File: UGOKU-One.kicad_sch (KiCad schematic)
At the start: 86 parts, among them J1 Conn_01x04, J10 Conn_01x02, J11 USB_C_Receptacle_USB2.0_16P, J12 Conn_01x02, J13 Conn_01x02, J2 SERVO, J3 Conn_02x03_Odd_Even, J4 Conn_01x10, J5 SERVO, J6 Conn_01x02, J8 DAC, J9 ADC, Q1 NMOS, Q2 SS8050, Q3 SS8050, SW1 SW_DIP_x02, SW2 SW_SPDT, SW4 SW_Push, SW6 SW_Push, U1 AMS1117-3.3, U2 CP2102N-A02-GQFN28, U3 TB67H450FNG_EL, U4 K7805M/M78AR05, U5 ESP32-WROOM-32E, U8 TB67H450FNG_EL

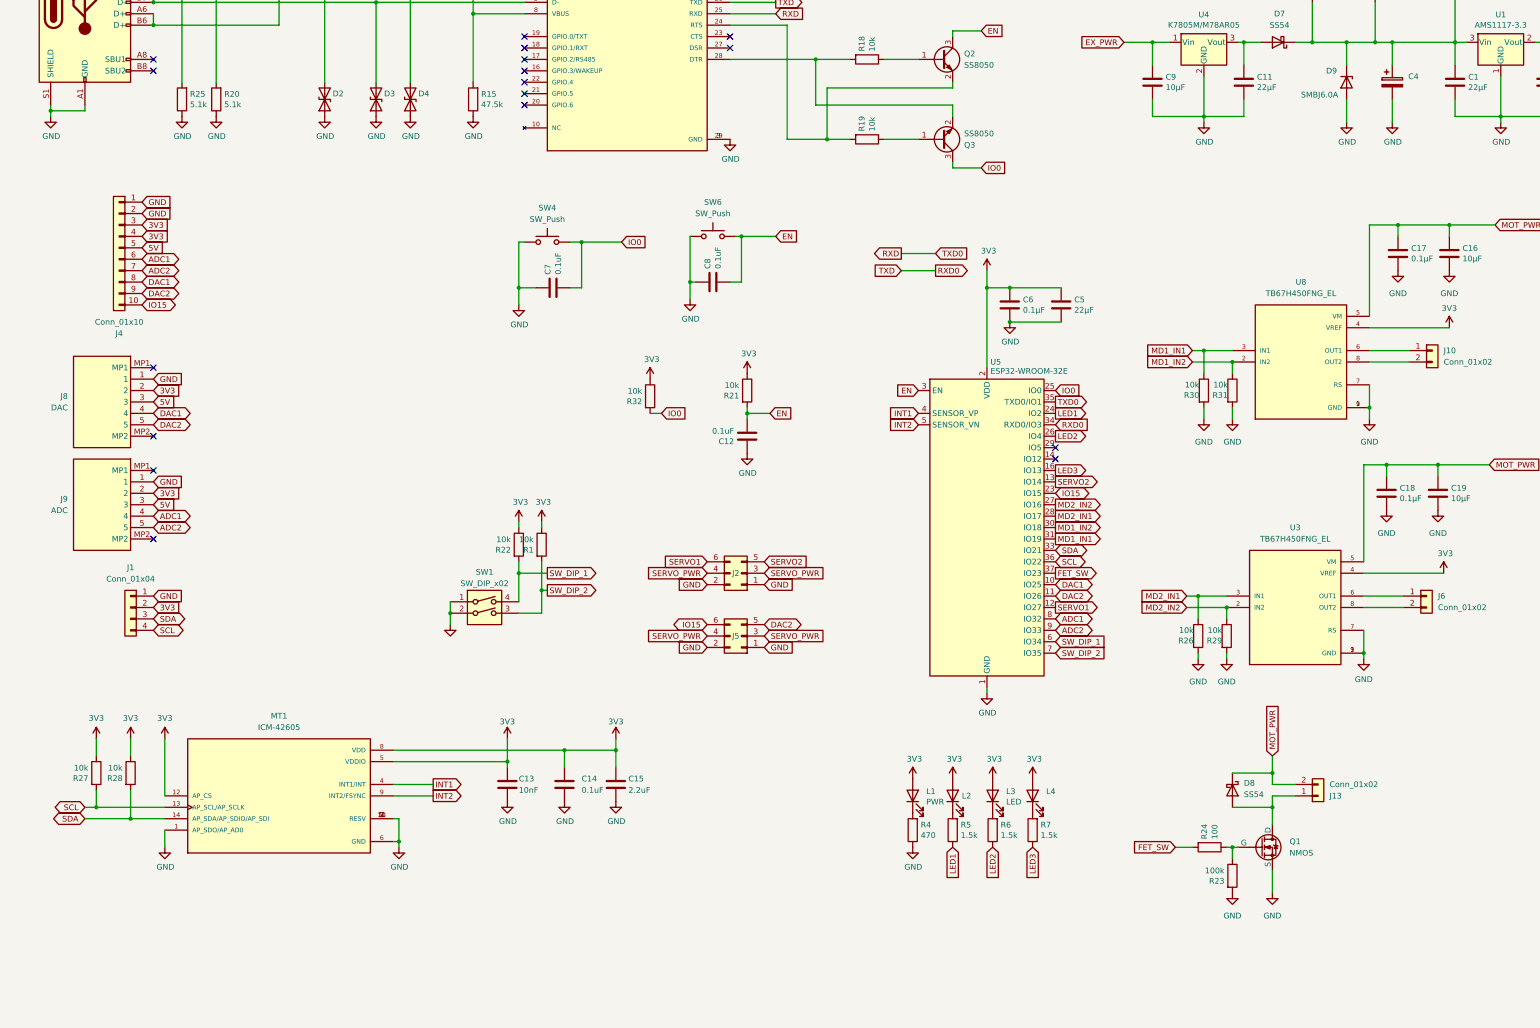
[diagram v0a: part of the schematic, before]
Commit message: 5VラインのコンデンサとTVSダイオードの配線を実施 IMUをBMI270に戻し
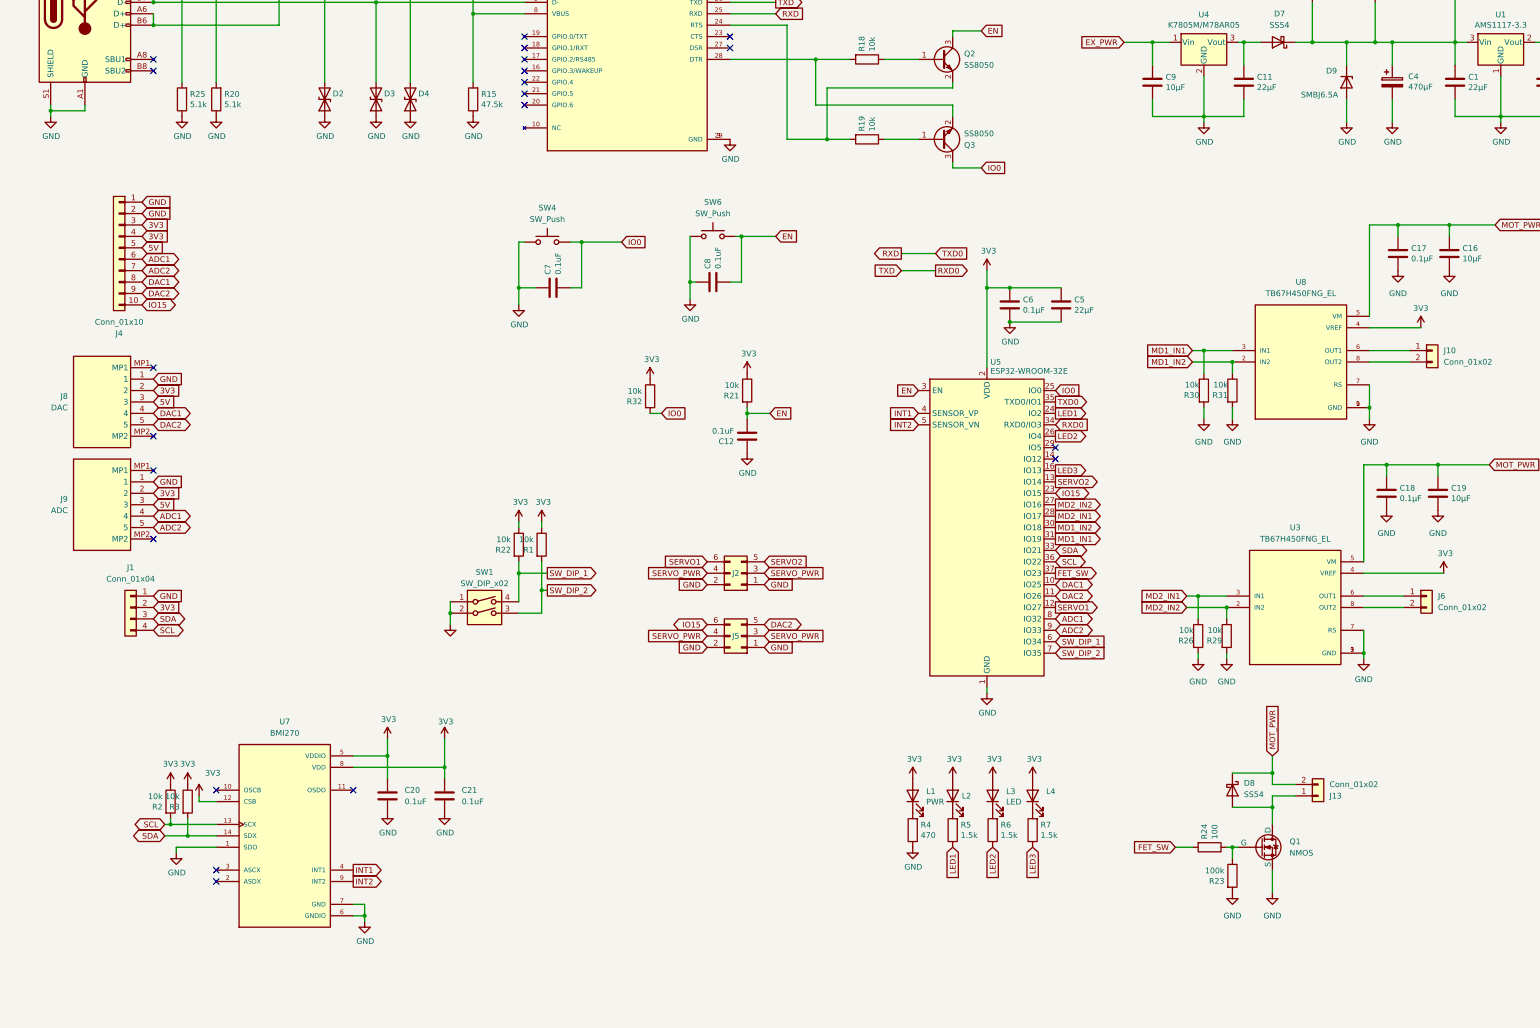
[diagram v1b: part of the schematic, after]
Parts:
- removed C13: 10nF, Capacitor_SMD:C_0402_1005Metric, symbol Device:C
- removed C14: 0.1uF, Capacitor_SMD:C_0402_1005Metric, symbol Device:C
- removed C15: 2.2uF, Capacitor_SMD:C_0402_1005Metric, symbol Device:C
- removed MT1: ICM-42605, 0_UGOKU-One_Lib:XDCR_ICM-42605, symbol ICM-42605:ICM-42605
- removed R27, R28: 10k, Resistor_SMD:R_0402_1005Metric, symbol Device:R
- added C20, C21: 0.1uF, Capacitor_SMD:C_0402_1005Metric, symbol Device:C
- added R2, R3: 10k, Resistor_SMD:R_0402_1005Metric, symbol Device:R
- added U7: BMI270, 0_UGOKU-One_Lib:XDCR_BMI270, symbol BMI270:BMI270
- C4: value C_Polarized -> 470μF; footprint Capacitor_SMD:CP_Elec_5x5.4 -> Capacitor_SMD:CP_Elec_6.3x7.7
- D9: value SMBJ6.0A -> SMBJ6.5A
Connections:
- net 3V3: now also C20.1, C21.1, R2.1, R3.1, U7.12 (CSB), U7.5 (VDDIO), U7.8 (VDD)
- net GND: now also C20.2, C21.2, U7.1 (SDO), U7.6 (GNDIO), U7.7 (GND)
- net INT1: now also U7.4 (INT1)
- net INT2: now also U7.9 (INT2)
- net SCL: now also R2.2, U7.13 (SCX)
- net SDA: now also R3.2, U7.14 (SDX)
- no-connect marks 24 -> 28

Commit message: ベタGNDとviaを修正
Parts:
- J4: footprint Connector_PinHeader_2.54mm:PinHeader_1x10_P2.54mm_Vertical -> Connector_PinSocket_2.54mm:PinSocket_1x10_P2.54mm_Vertical
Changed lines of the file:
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@@
 			)
 		)
-		(property "Footprint" "Connector_PinHeader_2.54mm:PinHeader_1x10_P2.54mm_Vertical"
+		(property "Footprint" "Connector_PinSocket_2.54mm:PinSocket_1x10_P2.54mm_Vertical"
 			(at 132.08 186.69 0)
 			(effects

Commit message: MD周りのベタ, viaを修正 BOM,CPLファイルを整備
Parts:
- C12, C20, C21, C3, C7, C8: value 0.1uF -> 0.1μF
- C2: value 22uF -> 22μF
- J2, J5: value SERVO -> Conn_02x03_Odd_Even
- J8: value DAC -> Harting-Conn
- J9: value ADC -> Harting-Conn
- L2: value IO2 -> LED
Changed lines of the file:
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@@
 			)
 		)
-		(property "Value" "IO2"
+		(property "Value" "LED"
 			(at 320.4972 309.9308 90)
 			(effects
@@
 			)
 		)
-		(property "Value" "SERVO"
+		(property "Value" "Conn_02x03_Odd_Even"
 			(at 269.24 266.7 0)
 			(effects
@@
 			)
 		)
-		(property "Value" "0.1uF"
+		(property "Value" "0.1μF"
 			(at 208.28 309.8799 0)
 			(effects
@@
 			)
 		)
-		(property "Value" "SERVO"
+		(property "Value" "Conn_02x03_Odd_Even"
 			(at 269.24 252.73 0)
 			(effects
@@
 			)
 		)
-		(property "Value" "22uF"
+		(property "Value" "22μF"
 			(at 279.4 102.8699 0)
 			(effects
@@
 			)
 		)
-		(property "Value" "0.1uF"
+		(property "Value" "0.1μF"
 			(at 290.83 102.8699 0)
 			(effects
@@
 		(on_board yes)
 		(dnp no)
-		(fields_autoplaced yes)
 		(property "Reference" "J9"
 			(at 120.65 242.5699 0)
@@
 			)
 		)
-		(property "Value" "ADC"
+		(property "Value" "Harting-Conn"
 			(at 120.65 245.1099 0)
 			(effects
@@
 			)
 		)
-		(property "Value" "DAC"
+		(property "Value" "Harting-Conn"
 			(at 120.65 222.2499 0)
 			(effects
@@
 			)
 		)
-		(property "Value" "0.1uF"
+		(property "Value" "0.1μF"
 			(at 265.303 191.389 0)
 			(effects
@@
 			)
 		)
-		(property "Value" "0.1uF"
+		(property "Value" "0.1μF"
 			(at 195.58 309.8799 0)
 			(effects
@@
 			)
 		)
-		(property "Value" "0.1uF"
+		(property "Value" "0.1μF"
 			(at 268.859 227.457 0)
 			(effects
@@
 			)
 		)
-		(property "Value" "0.1uF"
+		(property "Value" "0.1μF"
 			(at 229.743 192.659 0)
 			(effects

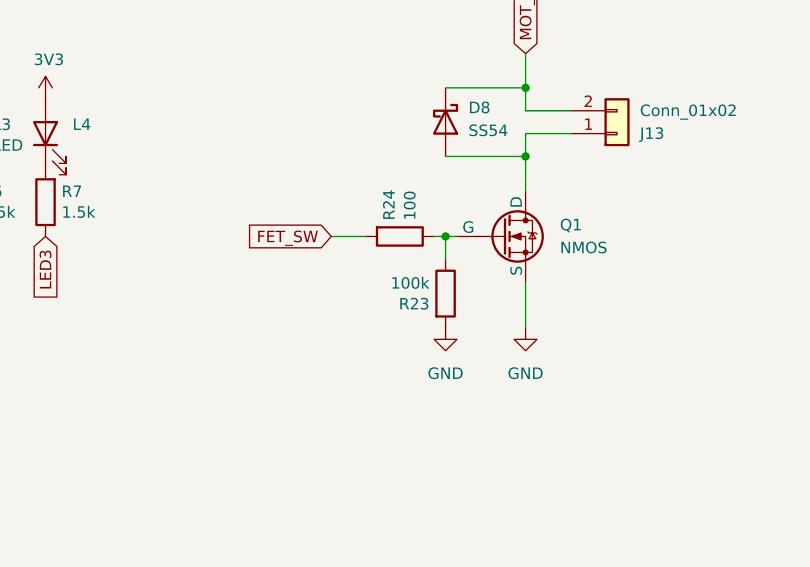
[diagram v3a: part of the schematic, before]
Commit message: コスト削減のため抵抗の種類を統一
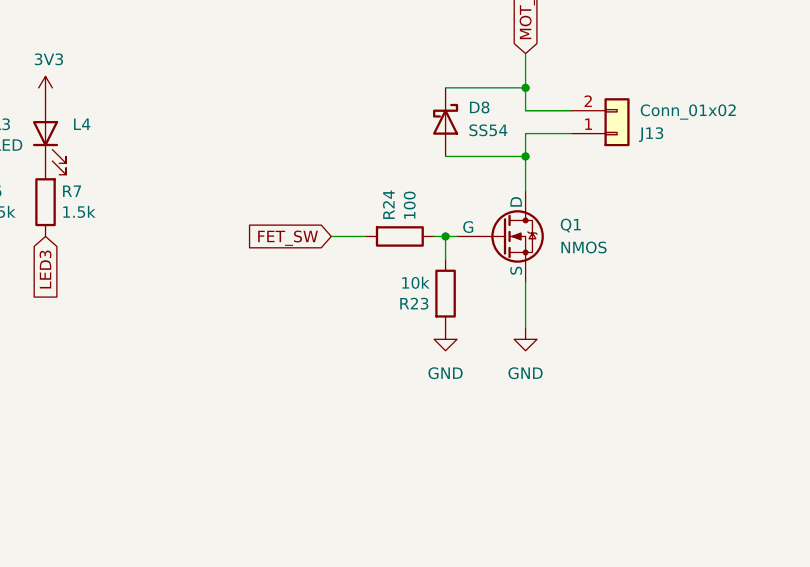
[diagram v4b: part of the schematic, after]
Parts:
- R13: footprint Resistor_SMD:R_0402_1005Metric -> Resistor_SMD:R_0603_1608Metric
- R23: value 100k -> 10k
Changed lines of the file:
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@@
 			)
 		)
-		(property "Value" "100k"
+		(property "Value" "10k"
 			(at 377.952 325.247 0)
 			(effects
@@
 			)
 		)
-		(property "Footprint" "Resistor_SMD:R_0402_1005Metric"
+		(property "Footprint" "Resistor_SMD:R_0603_1608Metric"
 			(at 218.948 99.06 90)
 			(effects

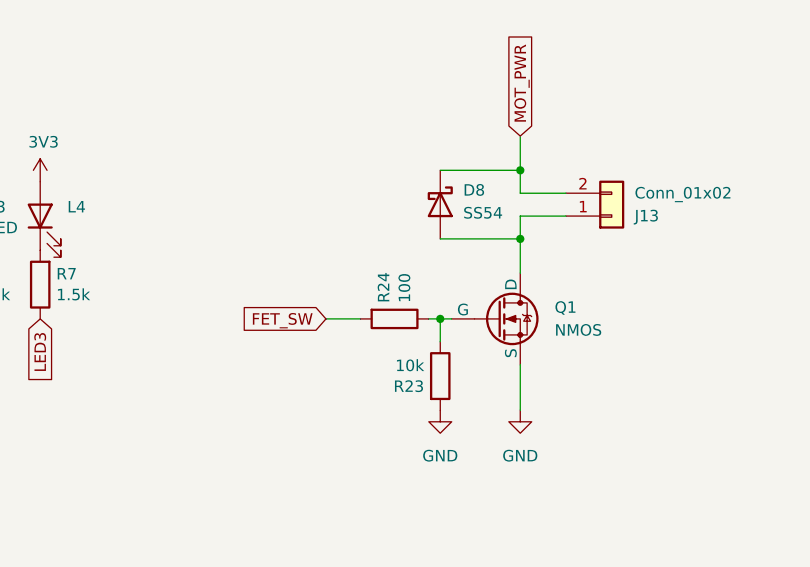
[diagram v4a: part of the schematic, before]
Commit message: 抵抗の種類削減
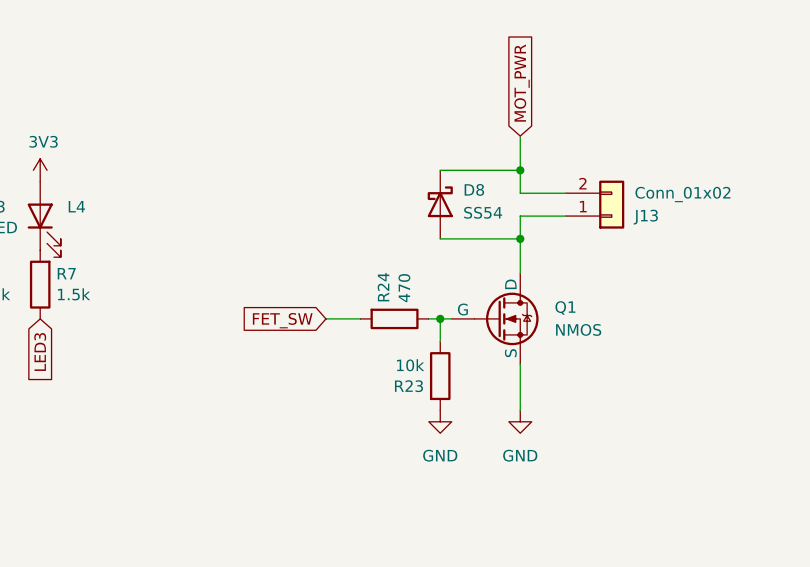
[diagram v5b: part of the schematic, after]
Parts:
- R24: value 100 -> 470; footprint Resistor_SMD:R_0402_1005Metric -> Resistor_SMD:R_0603_1608Metric
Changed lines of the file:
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@@
 			)
 		)
-		(property "Value" "100"
+		(property "Value" "470"
 			(at 375.793 318.262 0)
 			(effects
@@
 			)
 		)
-		(property "Footprint" "Resistor_SMD:R_0402_1005Metric"
+		(property "Footprint" "Resistor_SMD:R_0603_1608Metric"
 			(at 374.65 318.262 90)
 			(effects

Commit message: アノテーションを更新
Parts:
- renumbered C2 to C1, C8 to C10, C7 to C11, C6 to C12, C5 to C13, C12 to C14, C18 to C15, C19 to C16, C20 to C17, C21 to C18, C3 to C2, C9 to C3, C11 to C4, C4 to C5, C1 to C6, C10 to C7, C17 to C8, C16 to C9, D6 to D1, D5 to D2, D7 to D3, D9 to D4, D2 to D5, D3 to D6, D4 to D7, J3 to J1, J1 to J10, J5 to J11, J13 to J12, J12 to J2, J11 to J3, J10 to J5, J8 to J6, J9 to J7, J2 to J8, J6 to J9, Q2 to Q1, Q3 to Q2, Q1 to Q3, R13 to R1, R30 to R10, R31 to R11, R32 to R12, R22 to R13, R1 to R14, R26 to R15, R29 to R16, R2 to R17, R3 to R18, R4 to R19, R16 to R2, R5 to R20, R6 to R21, R7 to R22, R24 to R23, R23 to R24, R14 to R3, R18 to R4, R25 to R5, R20 to R6, R15 to R7, R19 to R8, R21 to R9, SW2 to SW1, SW6 to SW2, SW4 to SW3, SW1 to SW4, U2 to U1, U4 to U2, U1 to U3, U8 to U4, U3 to U6
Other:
- moved on the sheet: C15, C16, C3, C4, C7, D8, J12, J9, Q3, R15, R16, R23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

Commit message: IOピンのラベル名とアノテーション番号を修正
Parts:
- renumbered C17 to C1, C3 to C10, C4 to C11, C5 to C12, C15 to C13, C8 to C14, C16 to C15, C9 to C16, C6 to C17, C7 to C18, C18 to C2, C11 to C3, C10 to C4, C14 to C5, C1 to C6, C2 to C7, C12 to C8, C13 to C9, D5 to D1, D6 to D2, D7 to D3, D8 to D4, D3 to D5, D1 to D6, D4 to D7, D2 to D8, J3 to J1, J5 to J10, J9 to J11, J1 to J3, J6 to J5, J7 to J6, J10 to J7, J11 to J9, R17 to R1, R12 to R10, R9 to R11, R2 to R12, R4 to R13, R8 to R14, R19 to R15, R20 to R16, R21 to R17, R22 to R18, R10 to R19, R5 to R2, R15 to R20, R11 to R21, R16 to R22, R18 to R3, R6 to R4, R3 to R5, R7 to R6, R1 to R7, R13 to R8, R14 to R9, SW3 to SW2, SW2 to SW3, U7 to U4, U4 to U6, U6 to U7
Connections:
- net ADC1 renamed IO32
- net ADC2 renamed IO33
- net DAC1 renamed IO25
- net DAC2 renamed IO26
